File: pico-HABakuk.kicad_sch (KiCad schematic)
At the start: 34 parts, among them J1 USB_B_Micro, J2 Conn_01x02, J3 Conn_02x18_Odd_Even, J4 Conn_02x18_Odd_Even, U1 NCP1117-3.3_SOT223, U2 W25Q128JVS, U3 RP2040, Y1 ABM8-272-T3

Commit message: First changes in the sch and pcb
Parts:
- removed J3, J4: Conn_02x18_Odd_Even, Connector_PinHeader_2.54mm:PinHeader_2x18_P2.54mm_Vertical, symbol Connector_Generic:Conn_02x18_Odd_Even
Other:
- note removed: "IOs"
- company: Raspberry Pi Ltd -> Jakub Šerých, OK1SE
- title: RP2040 Minimal Design Example -> pico-HABakuk

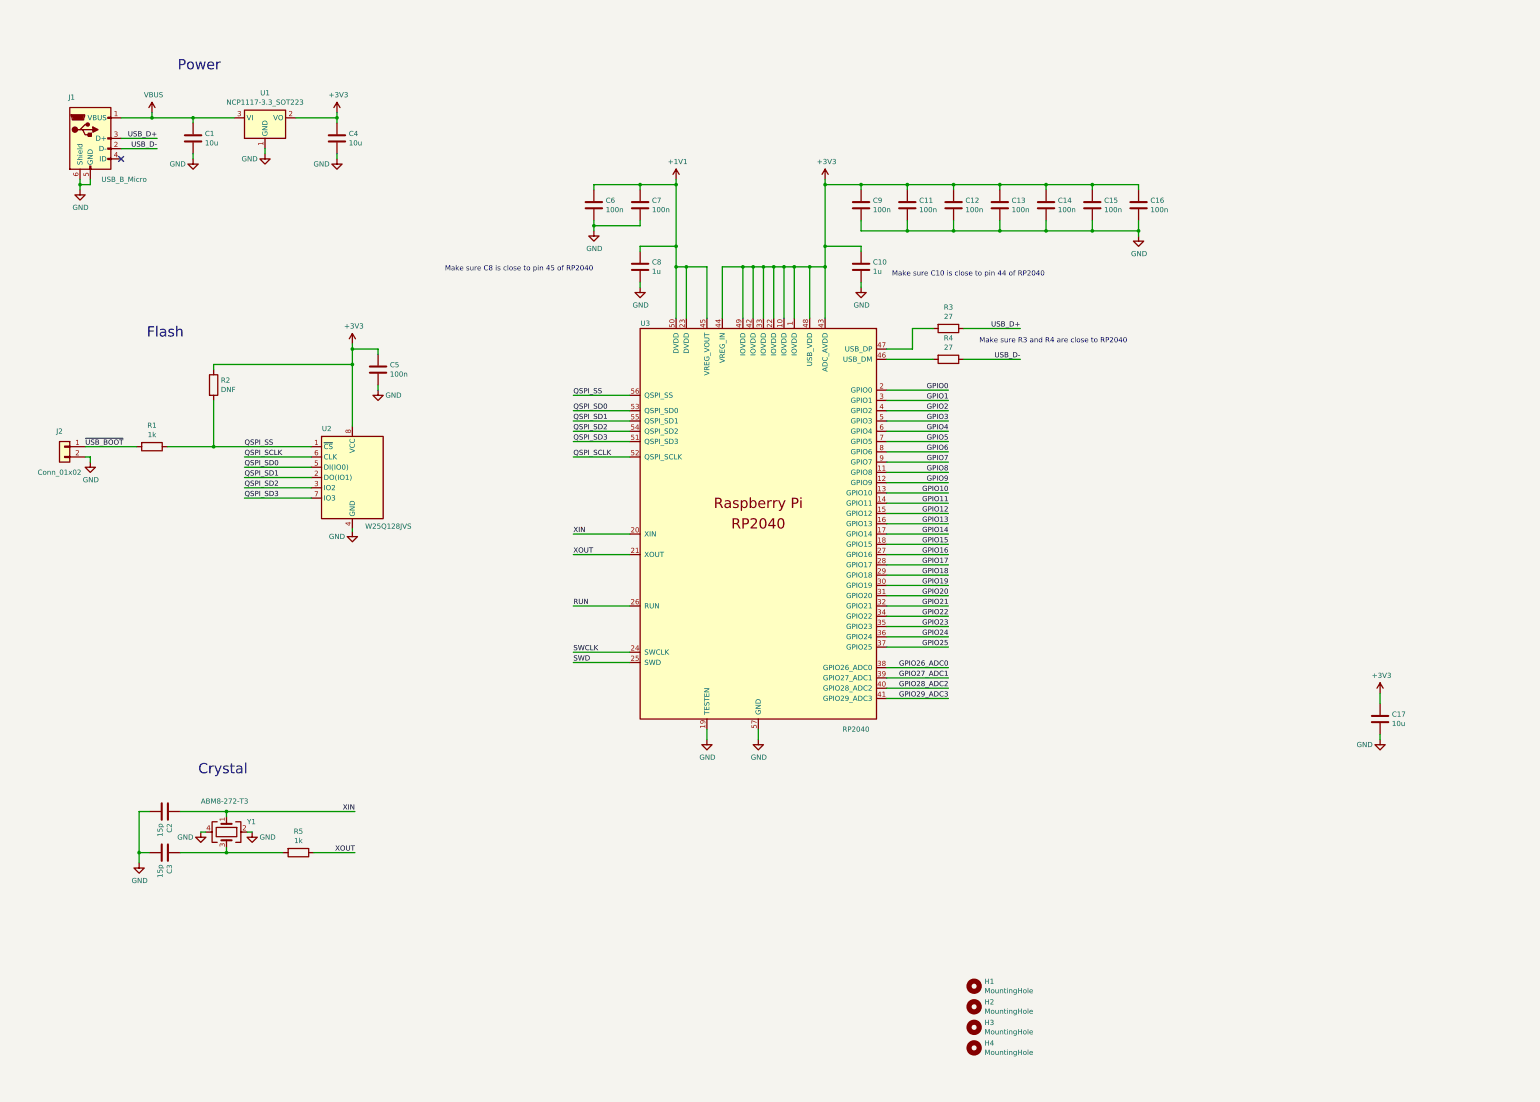
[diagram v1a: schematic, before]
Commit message: Solar MPPT regulator copied into schema
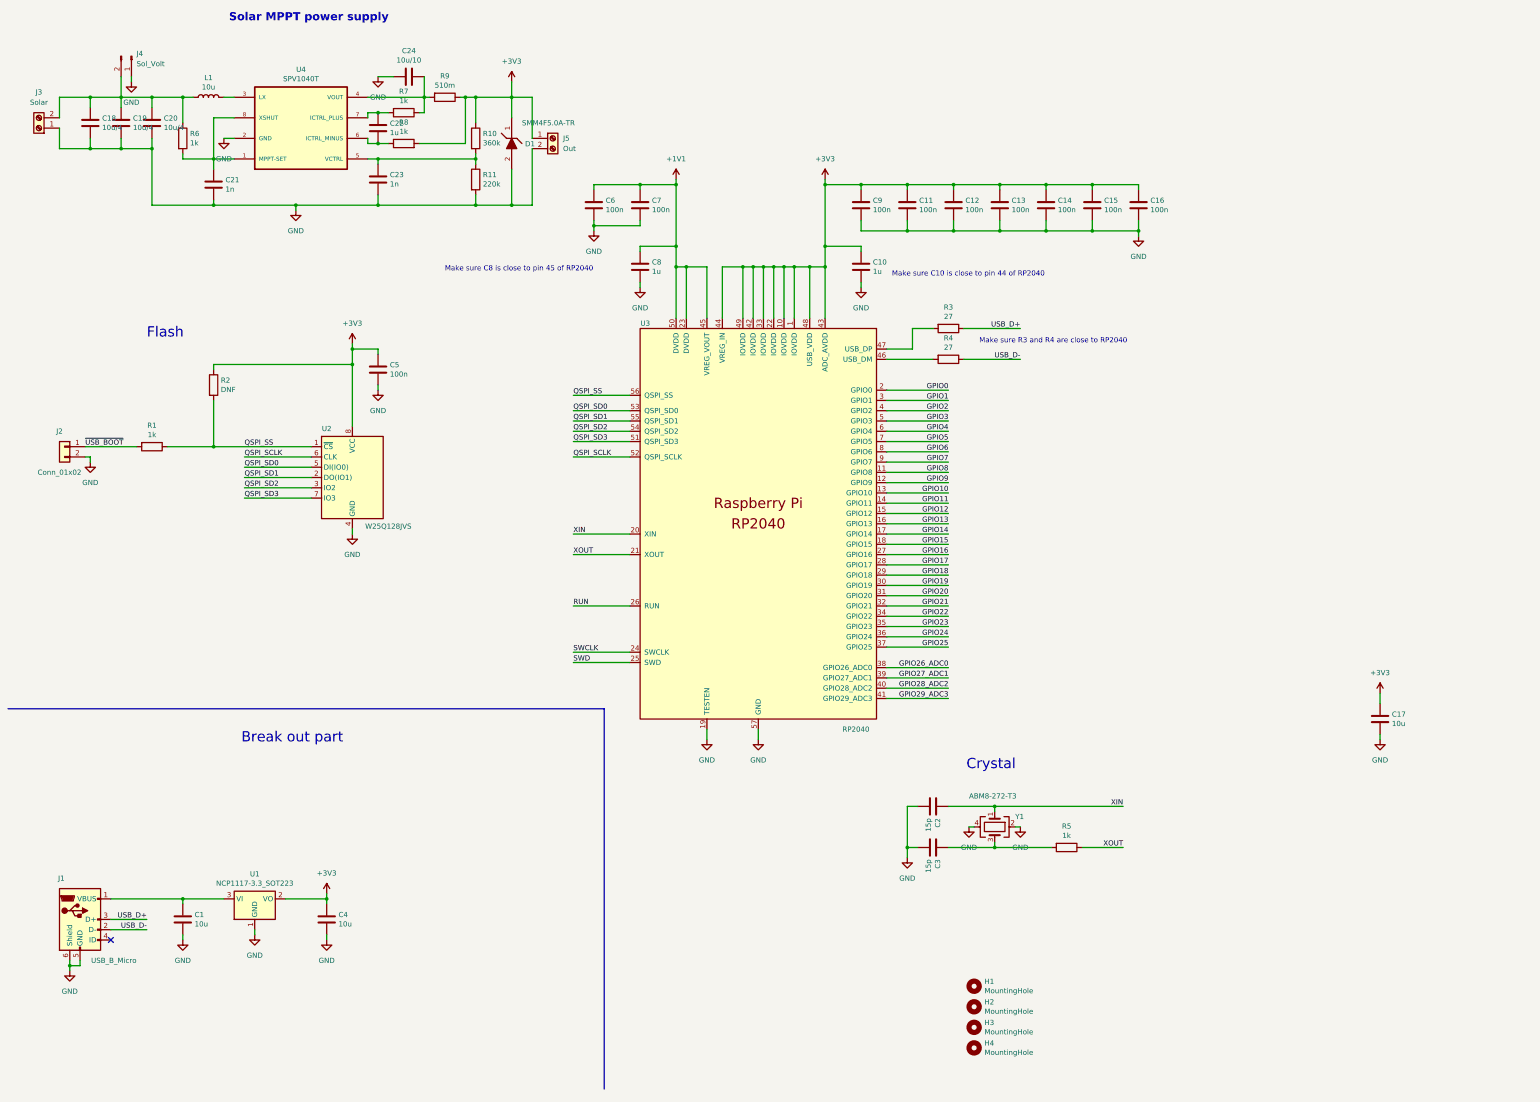
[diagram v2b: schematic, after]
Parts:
- added C18, C19, C20: 10u/4, Capacitor_SMD:C_0603_1608Metric, symbol Device:C
- added C21, C23: 1n, Capacitor_SMD:C_0603_1608Metric, symbol Device:C
- added C22: 1u, Capacitor_SMD:C_0603_1608Metric, symbol Device:C
- added C24: 10u/10, Capacitor_SMD:C_0805_2012Metric, symbol Device:C
- added D1: SMM4F5.0A-TR, _moje_footprints:STMITE, symbol SamacSys_Parts:SMM4F5.0A-TR
- added J3: Solar, TerminalBlock_4Ucon:TerminalBlock_4Ucon_1x02_P3.50mm_Vertical, symbol Connector:Screw_Terminal_01x02
- added J4: Sol_Volt, Connector_PinHeader_2.54mm:PinHeader_1x02_P2.54mm_Vertical, symbol Connector:Conn_01x02_Pin
- added J5: Out, TerminalBlock_4Ucon:TerminalBlock_4Ucon_1x02_P3.50mm_Vertical, symbol Connector:Screw_Terminal_01x02
- added L1: 10u, Inductor_SMD:L_Taiyo-Yuden_MD-3030, symbol Device:L
- added R10: 360k, Resistor_SMD:R_0603_1608Metric, symbol Device:R
- added R11: 220k, Resistor_SMD:R_0603_1608Metric, symbol Device:R
- added R6, R7, R8: 1k, Resistor_SMD:R_0603_1608Metric, symbol Device:R
- added R9: 510m, Resistor_SMD:R_0603_1608Metric, symbol Device:R
- added U4: SPV1040T, Package_SO:TSSOP-8_4.4x3mm_P0.65mm, symbol SPV1040T:SPV1040T
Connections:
- net +3V3: now also D1.1, J5.1 (Pin_1), R10.1, R8.2, R9.1
- net GND: now also C18.2, C19.2, C20.2, C21.2, C23.2, C24.2, D1.2, J3.1 (Pin_1), J4.1 (Pin_1), J5.2 (Pin_2), R11.2, U4.2 (GND)
- net VBUS: no longer names the net of C1.1, J1.1 (VBUS), U1.3 (VI)
- new net: C24.1, R7.1, R9.2, U4.4 (VOUT)
- new net: C21.1, R6.2, U4.1 (MPPT-SET), U4.8 (XSHUT)
- new net: L1.2, U4.3 (LX)
- new net: C23.1, R10.2, R11.1, U4.5 (VCTRL)
- new net: C22.2, R8.1, U4.6 (ICTRL_MINUS)
- new net: C22.1, R7.2, U4.7 (ICTRL_PLUS)
- new net: C18.1, C19.1, C20.1, J3.2 (Pin_2), J4.2 (Pin_2), L1.1, R6.1
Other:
- note added: "Break out part"
- note added: "Solar MPPT power supply"
- note removed: "Power"
- moved on the sheet: C1, C2, C3, C4, J1, R5, U1, Y1

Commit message: adding parts to schematics
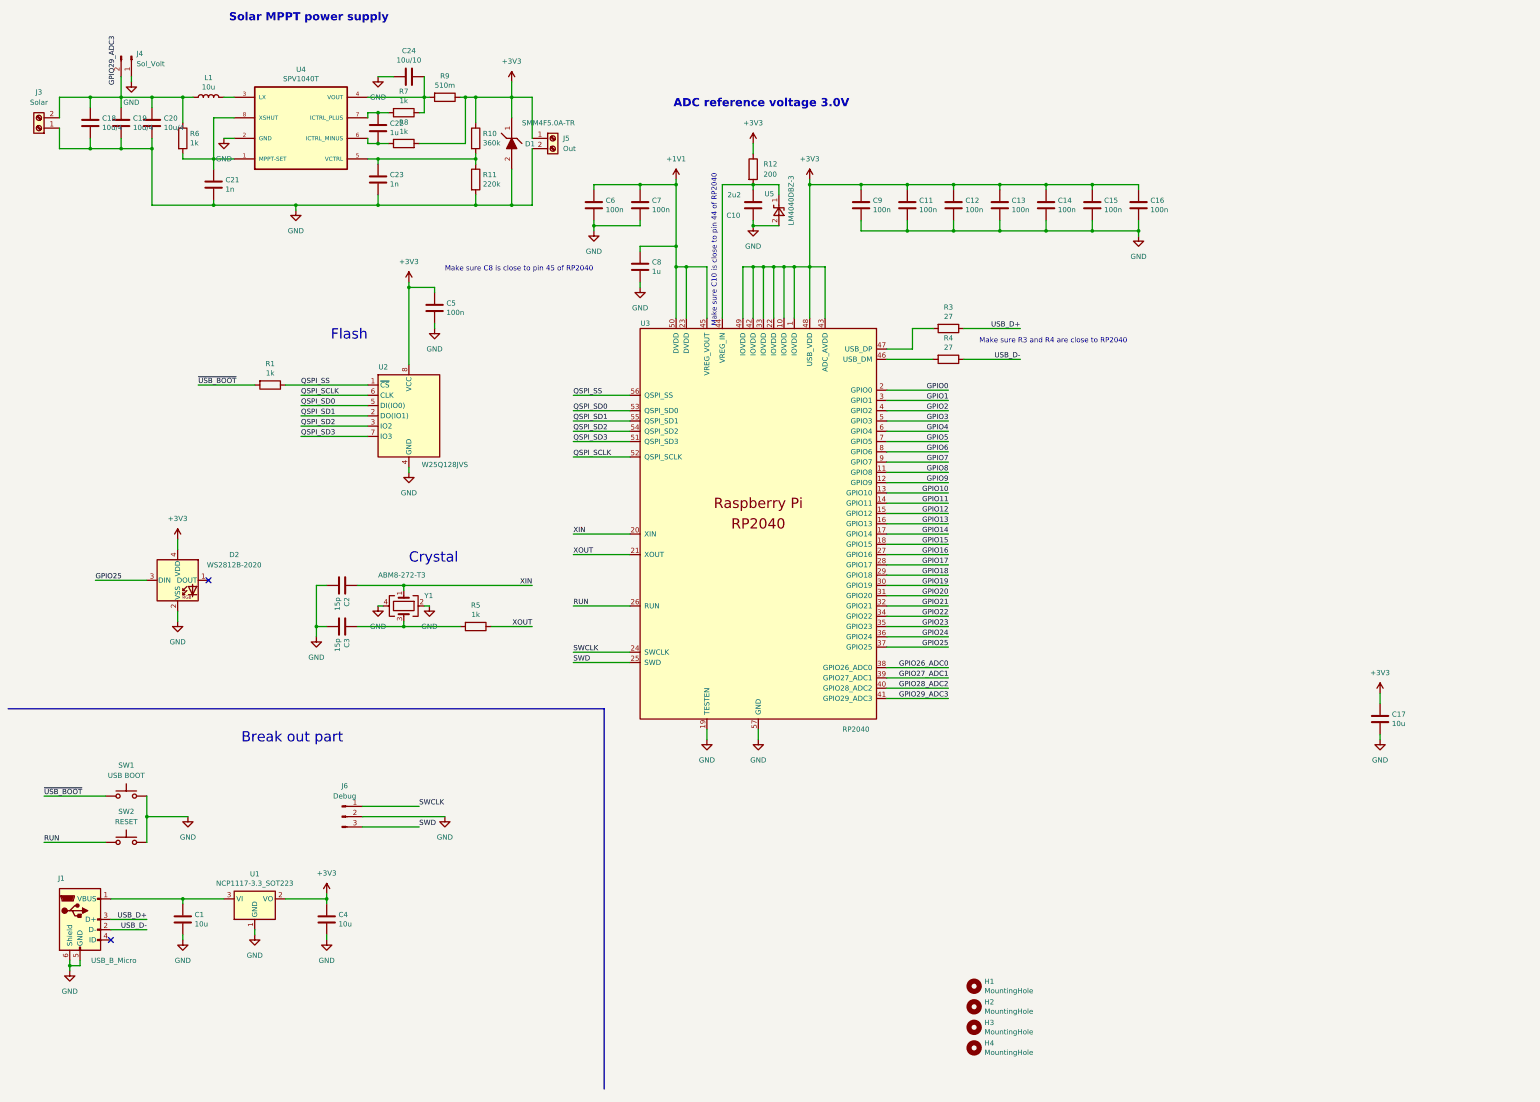
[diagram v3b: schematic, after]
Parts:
- removed J2: Conn_01x02, Connector_PinHeader_2.54mm:PinHeader_1x02_P2.54mm_Vertical, symbol Connector_Generic:Conn_01x02
- removed R2: DNF, Resistor_SMD:R_0402_1005Metric, symbol Device:R
- added D2: WS2812B-2020, LED_SMD:LED_WS2812B-2020_PLCC4_2.0x2.0mm, symbol LED:WS2812B-2020
- added J6: Debug, Connector_PinHeader_2.54mm:PinHeader_1x03_P2.54mm_Vertical, symbol Connector:Conn_01x03_Pin
- added R12: 200, symbol Device:R
- added SW1: USB BOOT, Button_Switch_SMD:SW_SPST_Omron_B3FS-100xP, symbol Switch:SW_Omron_B3FS
- added SW2: RESET, Button_Switch_SMD:SW_SPST_Omron_B3FS-100xP, symbol Switch:SW_Omron_B3FS
- added U5: LM4040DBZ-3, Package_TO_SOT_SMD:SOT-23, symbol Reference_Voltage:LM4040DBZ-3
- C10: value 1u -> 2u2
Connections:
- net +3V3: now also D2.4 (VDD), R12.1; no longer C10.1, U3.44 (VREG_IN)
- net GND: now also D2.2 (VSS), J6.2 (Pin_2), SW1.2, SW2.2, U5.2 (A)
- net GPIO25: now also D2.3 (DIN)
- net RUN: now also SW2.1
- net SWCLK: now also J6.1 (Pin_1)
- net SWD: now also J6.3 (Pin_3)
- net ~{USB_BOOT}: now also SW1.1
- new net: C10.1, R12.2, U3.44 (VREG_IN), U5.1 (K)
- no-connect marks 1 -> 2
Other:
- note added: "ADC reference voltage 3.0V"
- moved on the sheet: C10, C2, C3, C5, R1, R5, U2, Y1

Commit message: More work on schematics
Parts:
- removed H1, H2, H3, H4: MountingHole, MountingHole:MountingHole_2.7mm_M2.5, symbol Mechanical:MountingHole
- removed J3: Solar, TerminalBlock_4Ucon:TerminalBlock_4Ucon_1x02_P3.50mm_Vertical, symbol Connector:Screw_Terminal_01x02
- removed J4: Sol_Volt, Connector_PinHeader_2.54mm:PinHeader_1x02_P2.54mm_Vertical, symbol Connector:Conn_01x02_Pin
- removed J5: Out, TerminalBlock_4Ucon:TerminalBlock_4Ucon_1x02_P3.50mm_Vertical, symbol Connector:Screw_Terminal_01x02
- removed J6: Debug, Connector_PinHeader_2.54mm:PinHeader_1x03_P2.54mm_Vertical, symbol Connector:Conn_01x03_Pin
- added J2: Ant+, Connector_PinHeader_2.54mm:PinHeader_1x01_P2.54mm_Vertical, symbol Connector:Conn_01x01_Pin
- added J4: Ant-, Connector_PinHeader_2.54mm:PinHeader_1x01_P2.54mm_Vertical, symbol Connector:Conn_01x01_Pin
- added J5: Solar, Connector_PinSocket_2.54mm:PinSocket_1x02_P2.54mm_Vertical, symbol Connector:Conn_01x02_Pin
- added J7: Ultra_Cap, Connector_PinSocket_2.54mm:PinSocket_1x02_P2.54mm_Vertical, symbol Connector:Conn_01x02_Pin
- added JP1: Solar_voltage, Jumper:SolderJumper-2_P1.3mm_Bridged_RoundedPad1.0x1.5mm, symbol Jumper:SolderJumper_2_Bridged
- added TP1: +3V3, Connector_Pin:Pin_D1.1mm_L8.5mm_W2.5mm_FlatFork, symbol Connector:TestPoint
- added TP2: USB_D+, Connector_Pin:Pin_D1.1mm_L8.5mm_W2.5mm_FlatFork, symbol Connector:TestPoint
- added TP3: USB_D-, Connector_Pin:Pin_D1.1mm_L8.5mm_W2.5mm_FlatFork, symbol Connector:TestPoint
- added TP4: GND, Connector_Pin:Pin_D1.1mm_L8.5mm_W2.5mm_FlatFork, symbol Connector:TestPoint
- added TP5: USB_BOOT, Connector_Pin:Pin_D1.1mm_L8.5mm_W2.5mm_FlatFork, symbol Connector:TestPoint
- added TP6: Reset, Connector_Pin:Pin_D1.1mm_L8.5mm_W2.5mm_FlatFork, symbol Connector:TestPoint
- added TP7: SWCLK, Connector_Pin:Pin_D1.1mm_L8.5mm_W2.5mm_FlatFork, symbol Connector:TestPoint
- added TP8: SWD, Connector_Pin:Pin_D1.1mm_L8.5mm_W2.5mm_FlatFork, symbol Connector:TestPoint
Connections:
- net +3V3: now also J7.1 (Pin_1), TP1.1
- net GND: now also J5.2 (Pin_2), J7.2 (Pin_2), TP4.1
- net GPIO28_ADC2: now also JP1.2 (B)
- net GPIO6: now also J2.1 (Pin_1)
- net GPIO7: now also J4.1 (Pin_1)
- net RUN: now also TP6.1
- net SWCLK: now also TP7.1
- net SWD: now also TP8.1
- net USB_D+: now also TP2.1
- net USB_D-: now also TP3.1
- net ~{USB_BOOT}: now also TP5.1
- net Solar+: now reaches C18.1, C19.1, C20.1, L1.1, R6.1
- net Solar+: now also J5.1 (Pin_1), JP1.1 (A)
- net XIN: no longer names the net of C2.1, U3.20 (XIN), Y1.1
- net XOUT: no longer names the net of R5.1, U3.21 (XOUT)
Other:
- note removed: "Crystal"
- moved on the sheet: C17, C2, C3, D2, R5, Y1

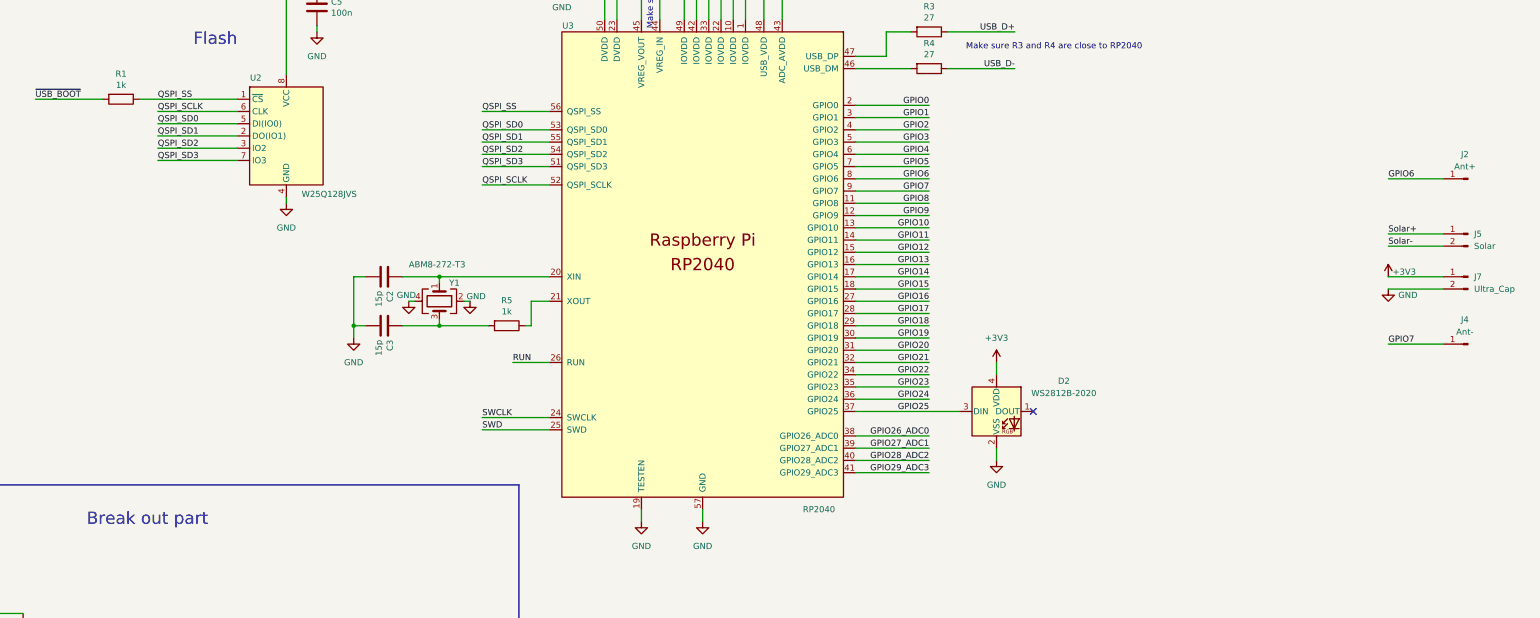
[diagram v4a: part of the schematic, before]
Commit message: GPS module added to schematics
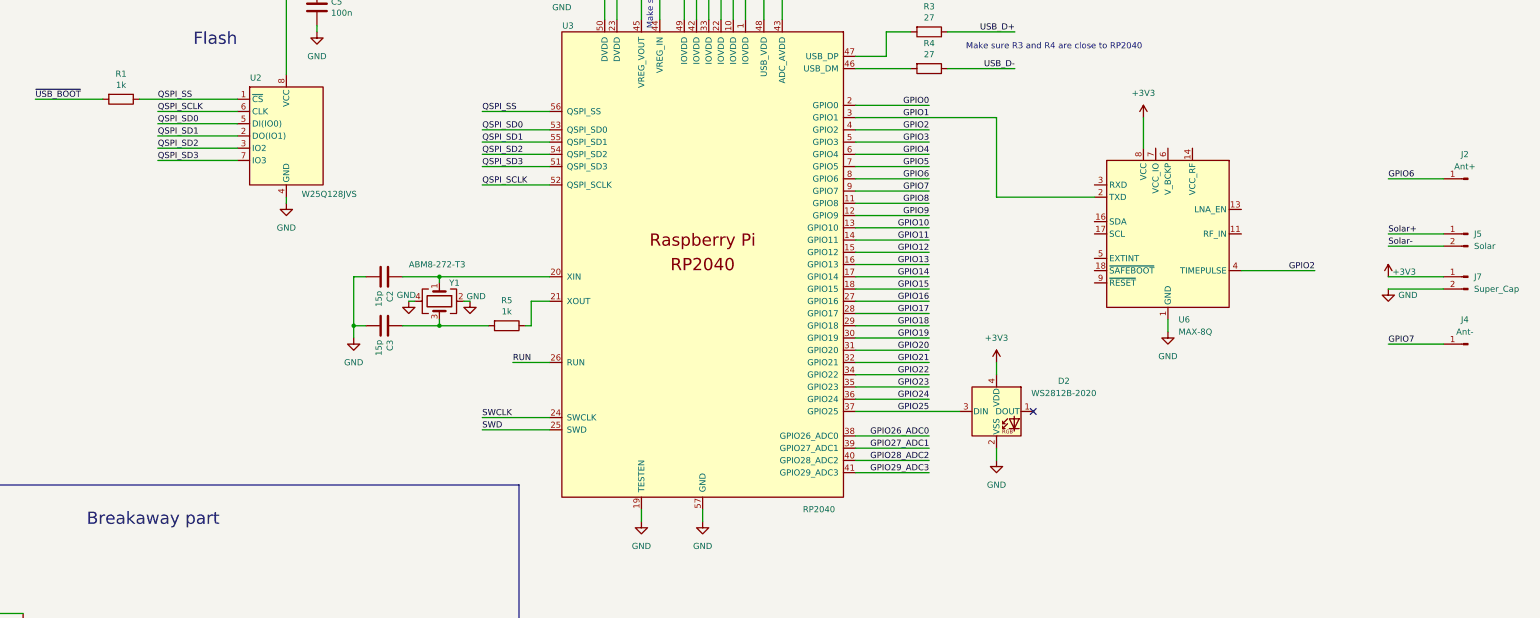
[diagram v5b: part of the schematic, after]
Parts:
- added U6: MAX-8Q, RF_GPS:ublox_MAX, symbol RF_GPS:MAX-8Q
- J7: value Ultra_Cap -> Super_Cap
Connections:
- net +3V3: now also U6.8 (VCC)
- net GND: now also U6.1 (GND), U6.10 (GND), U6.12 (GND)
- net GPIO1: now also U6.2 (TXD)
- net GPIO2: now also U6.4 (TIMEPULSE)
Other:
- note added: "Breakaway part"
- note removed: "Break out part"
